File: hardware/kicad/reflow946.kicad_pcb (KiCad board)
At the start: 2 copper layers, 104 x 60 mm, 56 parts, among them J1 VH-2A, J2 VH-3A2, J3 VH-3A2, J4 XH-A2, J5 HDR-M-2.54_2x3, Q1 BTA16-600BRG, Q2 MMBT3906, Q3 MMBT3906, Q4 MMBT3906, SW1 SW_Push, SW2 SW_Push, SW3 SW_Push, U1 MOC3041M, U2 ESP32-WROOM-32U, U3 MAX31855KASA, U4 AMS1117-3.3

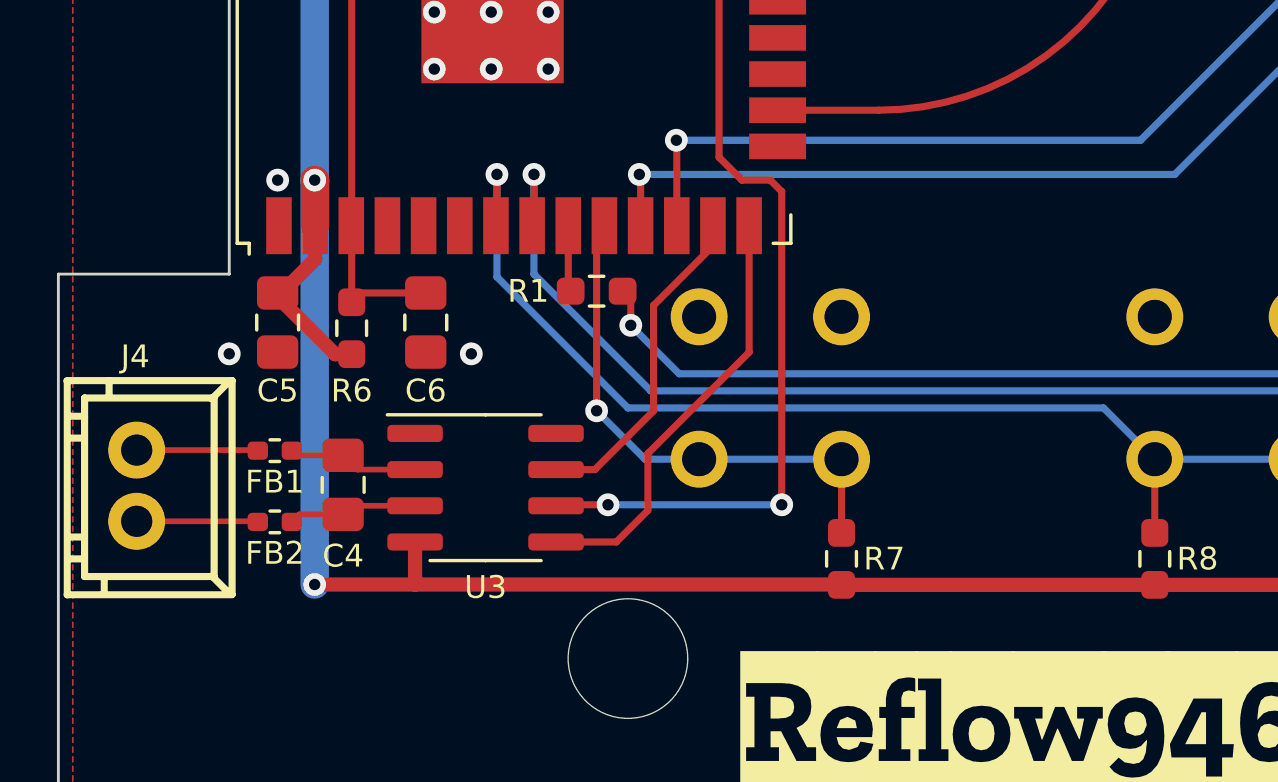
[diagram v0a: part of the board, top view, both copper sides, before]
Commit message: Use 0603 ferrite beads
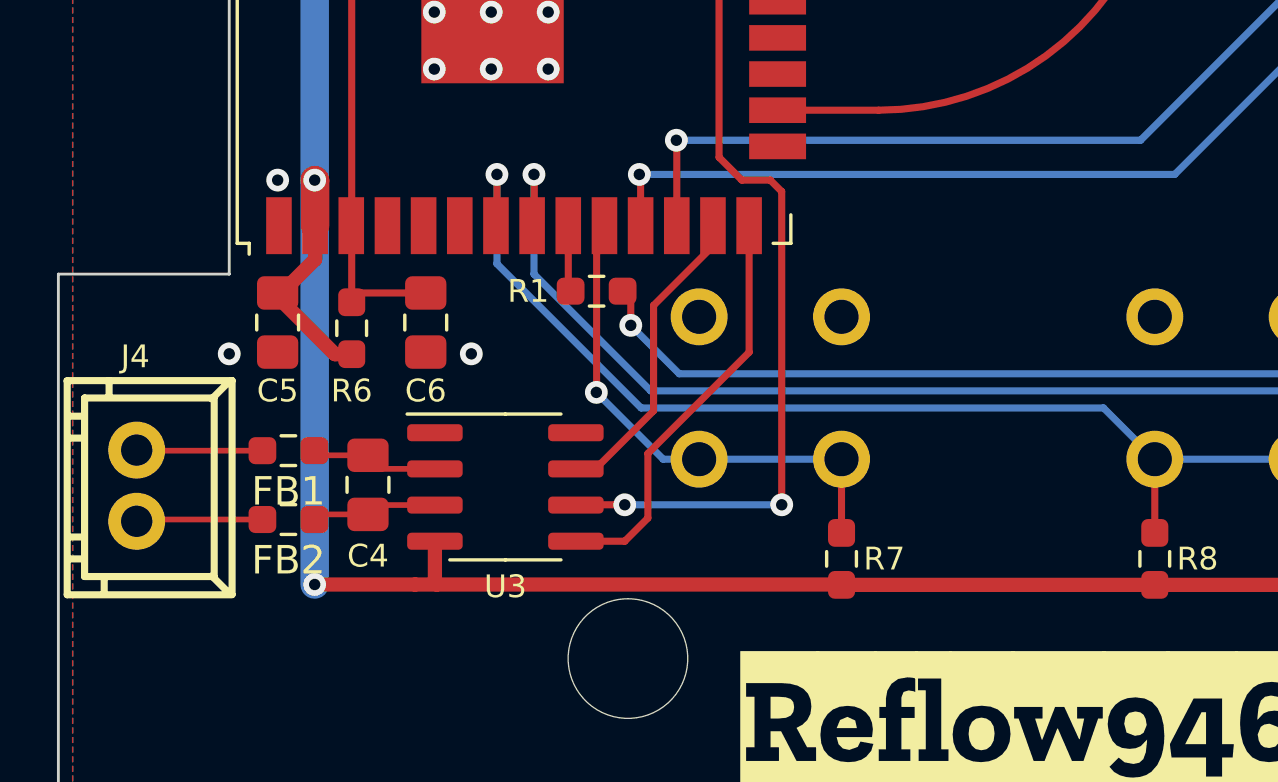
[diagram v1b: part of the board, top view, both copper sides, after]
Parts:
- FB1, FB2: footprint Resistor_SMD:R_0402_1005Metric_Pad0.72x0.64mm_HandSolder -> Resistor_SMD:R_0603_1608Metric_Pad0.98x0.95mm_HandSolder
- moved C4 0.87 mm to (110.9, 117.4)
- moved U3 0.70 mm to (115.7, 117.5)
- moved FB2 0.48 mm to (108.1, 118.6)
- moved FB1 0.48 mm to (108.1, 116.2)
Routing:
- net /MISO: track 11.6 -> 10.9 mm
- net /CS: track 33.8 -> 33.1 mm
- net /CLK: track 15.2 -> 14.6 mm
